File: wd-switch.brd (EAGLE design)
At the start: 35.2 x 57.1 mm, 13 parts, among them Q1 BC337, Q2 IRF530, Q3 IRF530

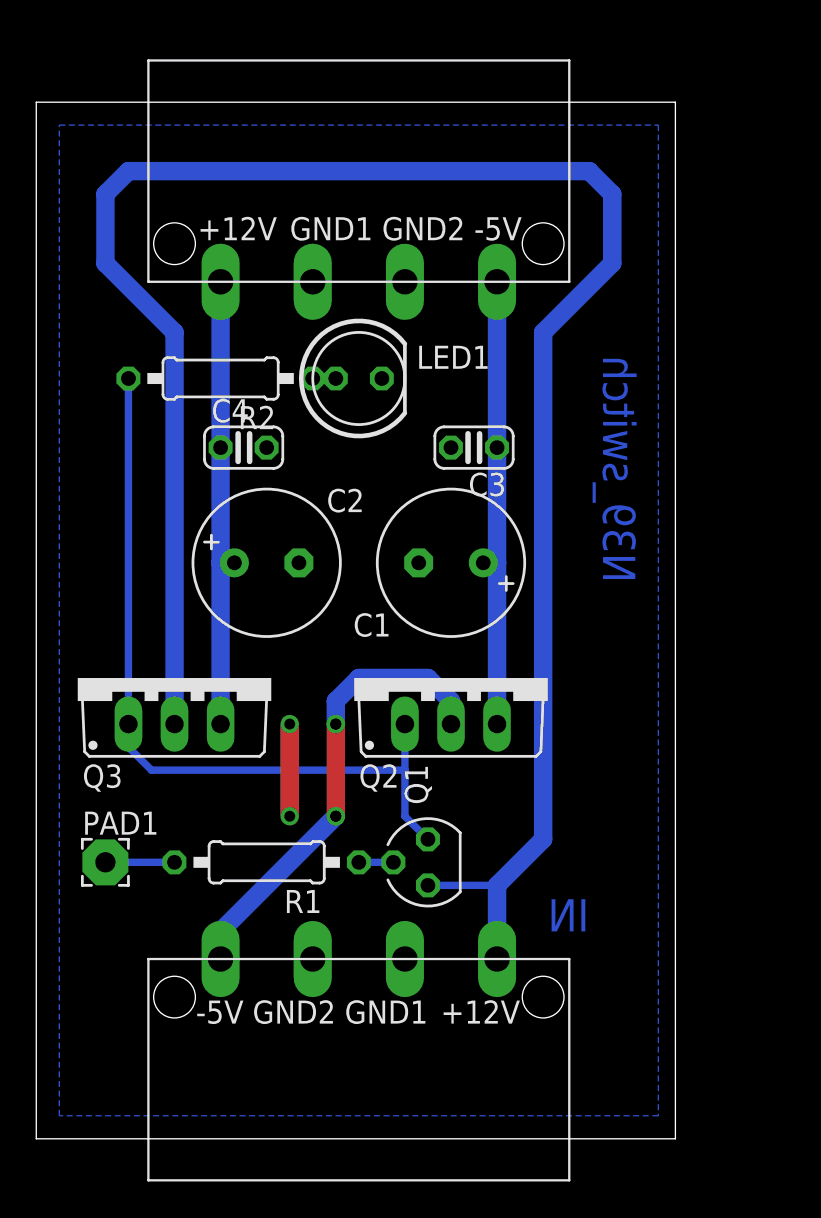
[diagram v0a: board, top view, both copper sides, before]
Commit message: * Bohrlöcher xD * kleine Verbesserungen im Platinenlayout
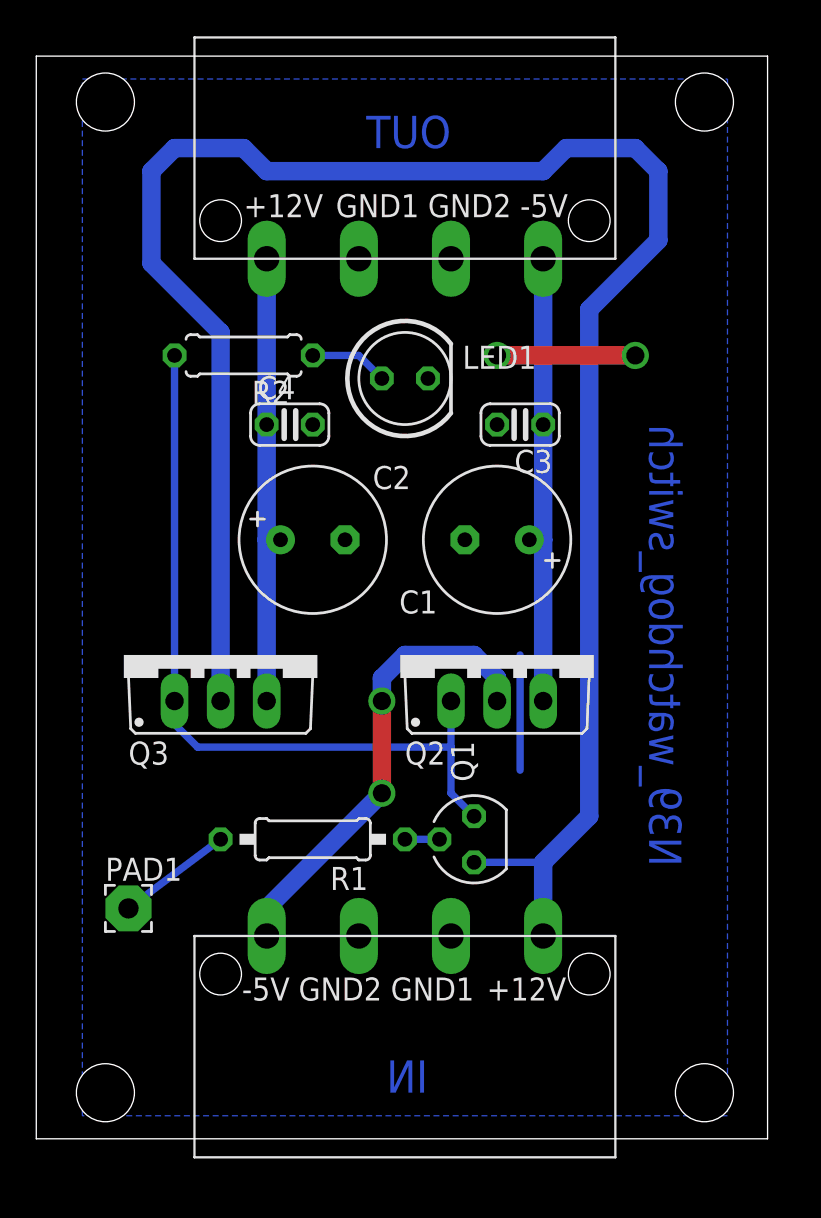
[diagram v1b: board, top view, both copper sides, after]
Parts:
- R2: device resistor:0207/10 -> resistor:0207/7
- moved C2 2.84 mm to (15.2, 33.0)
- moved R1 2.84 mm to (15.2, 16.5)
- moved Q3 2.84 mm to (10.2, 26.7)
- moved PAD1 2.84 mm to (5.08, 12.7)
- moved C1 2.84 mm to (25.4, 33.0)
- moved C3 2.84 mm to (26.7, 39.4)
- moved Q2 2.84 mm to (25.4, 26.7)
- moved Q1 2.84 mm to (24.1, 16.5)
- moved C4 2.84 mm to (14.0, 39.4)
- moved U$1 2.84 mm to (20.3, 5.08)
- moved U$2 2.84 mm to (20.3, 54.6)
- moved LED1 2.54 mm to (20.3, 41.9)
- moved R2 1.80 mm to (11.4, 43.2)
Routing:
- net GND: track 5.08 -> 14.0 mm
- net N$7: track 1.27 -> 4.34 mm
- net N$5: track 3.81 -> 6.35 mm
- net VCC: track 108.4 -> 109.4 mm
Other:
- board size 35.2 x 57.1 mm -> 40.3 x 59.7 mm
- board text added: "N39_watchdog_switch"
- board text added: "OUT"
- board text removed: "N39_switch"

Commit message: Pinheaders für statische Schalterstellung
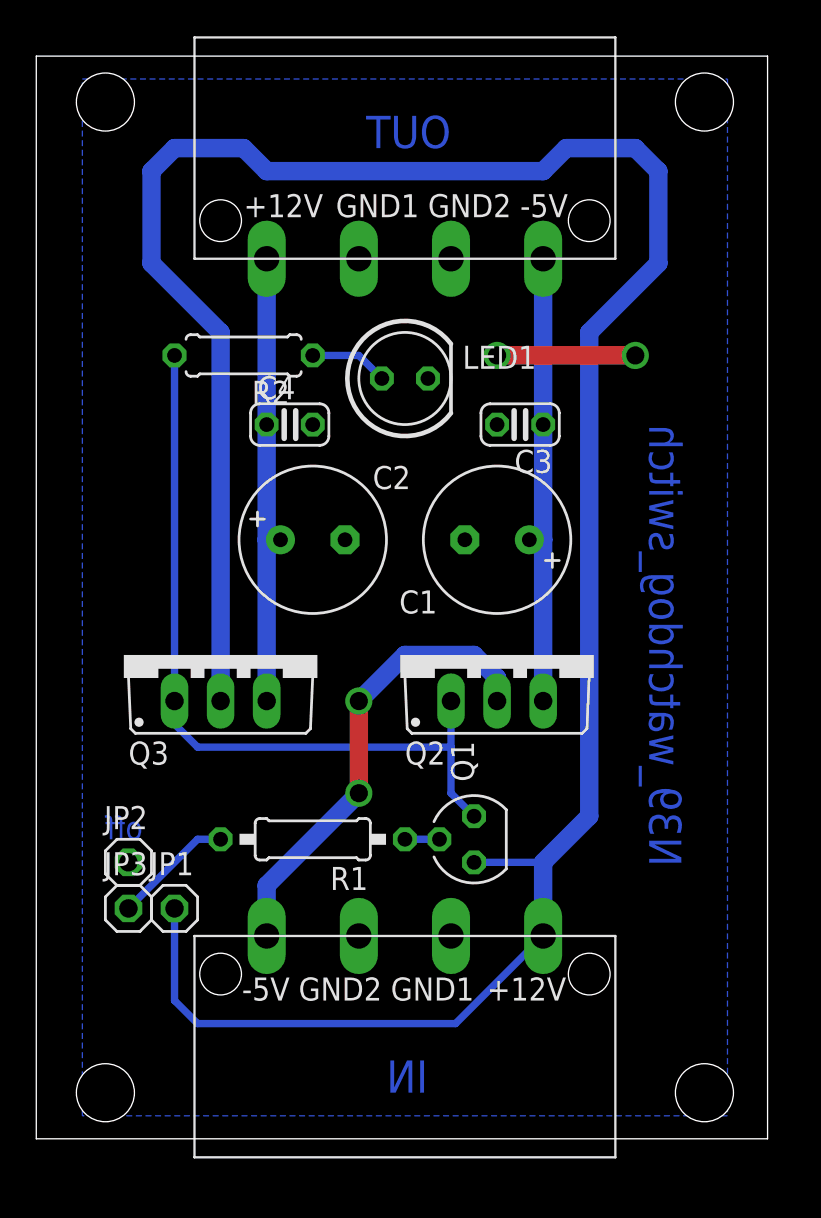
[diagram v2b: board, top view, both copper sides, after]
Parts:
- removed PAD1: WIREPAD2,54/1,1, wirepad:2,54/1,1
- added JP1: ON, pinhead:1X01
- added JP2: OFF, pinhead:1X01
- added JP3: IN, pinhead:1X01
- LED1: value (none) -> GN
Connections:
- net GND: now also JP2.1
- net N$5: now also JP3.1; no longer PAD1.1
- net VCC: now also JP1.1
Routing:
- net VCC: track 109.4 -> 137.4 mm
- net GND: track 14.0 -> 7.62 mm
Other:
- board text added: "off"
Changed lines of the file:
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@@
 <setting verticaltext="up"/>
 </settings>
-<grid distance="0.05" unitdist="inch" unit="inch" style="lines" multiple="1" display="no" altdistance="0.025" altunitdist="inch" altunit="inch"/>
+<grid distance="1.27" unitdist="mm" unit="mm" style="lines" multiple="1" display="no" altdistance="0.025" altunitdist="inch" altunit="inch"/>
 <layers>
 <layer number="1" name="Top" color="4" fill="1" visible="yes" active="yes"/>
@@
 <text x="22.86" y="54.61" size="1.778" layer="16" font="vector" rot="MR0">OUT</text>
 <text x="35.56" y="39.37" size="1.778" layer="16" font="vector" rot="MR270">N39_watchdog_switch</text>
+<text x="3.81" y="17.78" size="1.27" layer="16" font="vector" rot="MR180">off</text>
 </plain>
 <attributes>
@@
 <element name="U$2" library="n39" package="PSW_5" value="" x="20.32" y="54.61"/>
 <element name="R1" library="resistor" package="0207/10" value="330R" x="15.24" y="16.51" rot="R180"/>
-<element name="PAD1" library="wirepad" package="2,54/1,1" value="WIREPAD2,54/1,1" x="5.08" y="12.7"/>
-<element name="LED1" library="led" package="LED5MM" value="" x="20.32" y="41.91"/>
+<element name="LED1" library="led" package="LED5MM" value="GN" x="20.32" y="41.91"/>
 <element name="R2" library="resistor" package="0207/7" value="150R" x="11.43" y="43.18" rot="R180"/>
 <element name="C1" library="resistor" package="E3,5-8" value="" x="25.4" y="33.02" rot="R180"/>
@@
 <element name="C3" library="resistor" package="C025-024X044" value="" x="26.67" y="39.37" rot="R180"/>
 <element name="C4" library="resistor" package="C025-024X044" value="" x="13.97" y="39.37"/>
+<element name="JP1" library="pinhead" package="1X01" value="ON" x="7.62" y="12.7"/>
+<element name="JP2" library="pinhead" package="1X01" value="OFF" x="5.08" y="15.24"/>
+<element name="JP3" library="pinhead" package="1X01" value="IN" x="5.08" y="12.7"/>
 </elements>
 <signals>
@@
 <wire x1="6.35" y1="53.34" x2="7.62" y2="54.61" width="1.016" layer="16"/>
 <wire x1="33.02" y1="54.61" x2="34.29" y2="53.34" width="1.016" layer="16"/>
-<wire x1="34.29" y1="53.34" x2="34.29" y2="49.53" width="1.016" layer="16"/>
-<wire x1="34.29" y1="49.53" x2="30.48" y2="45.72" width="1.016" layer="16"/>
-<wire x1="30.48" y1="45.72" x2="30.48" y2="17.78" width="1.016" layer="16"/>
+<wire x1="34.29" y1="53.34" x2="34.29" y2="48.26" width="1.016" layer="16"/>
+<wire x1="34.29" y1="48.26" x2="30.48" y2="44.45" width="1.016" layer="16"/>
+<wire x1="30.48" y1="44.45" x2="30.48" y2="17.78" width="1.016" layer="16"/>
 <wire x1="30.48" y1="17.78" x2="27.94" y2="15.24" width="1.016" layer="16"/>
 <wire x1="27.94" y1="15.24" x2="27.94" y2="11.18" width="1.016" layer="16"/>
@@
 <wire x1="27.94" y1="53.34" x2="29.21" y2="54.61" width="1.016" layer="16"/>
 <wire x1="29.21" y1="54.61" x2="33.02" y2="54.61" width="1.016" layer="16"/>
+<contactref element="JP1" pad="1"/>
+<wire x1="7.62" y1="12.7" x2="7.62" y2="7.62" width="0.4064" layer="16"/>
+<wire x1="7.62" y1="7.62" x2="8.89" y2="6.35" width="0.4064" layer="16"/>
+<wire x1="8.89" y1="6.35" x2="23.11" y2="6.35" width="0.4064" layer="16"/>
+<wire x1="23.11" y1="6.35" x2="27.94" y2="11.18" width="0.4064" layer="16"/>
 </signal>
 <signal name="GND">
@@
 <via x="25.4" y="43.18" extent="1-16" drill="1" diameter="1.4224"/>
 <wire x1="25.4" y1="43.18" x2="33.02" y2="43.18" width="1.016" layer="1"/>
-<wire x1="26.67" y1="26.67" x2="26.67" y2="20.32" width="0.4064" layer="16"/>
+<contactref element="JP2" pad="1"/>
 </signal>
 <signal name="N$1">
@@
 <wire x1="25.4" y1="25.4" x2="24.13" y2="26.67" width="1.016" layer="16"/>
 <wire x1="24.13" y1="26.67" x2="20.32" y2="26.67" width="1.016" layer="16"/>
-<wire x1="20.32" y1="26.67" x2="19.05" y2="25.4" width="1.016" layer="16"/>
-<wire x1="19.05" y1="25.4" x2="19.05" y2="24.13" width="1.016" layer="16"/>
-<via x="19.05" y="24.13" extent="1-16" drill="0.6" shape="square"/>
-<wire x1="19.05" y1="24.13" x2="19.05" y2="19.05" width="1.016" layer="1"/>
-<via x="19.05" y="19.05" extent="1-16" drill="0.6" shape="square"/>
-<wire x1="19.05" y1="19.05" x2="12.7" y2="12.7" width="1.016" layer="16"/>
-<wire x1="12.7" y1="12.7" x2="12.7" y2="11.18" width="1.016" layer="16"/>
+<wire x1="20.32" y1="26.67" x2="17.78" y2="24.13" width="1.016" layer="16"/>
+<via x="17.78" y="24.13" extent="1-16" drill="0.6" shape="square"/>
+<wire x1="17.78" y1="24.13" x2="17.78" y2="19.05" width="1.016" layer="1"/>
+<via x="17.78" y="19.05" extent="1-16" drill="0.6" shape="square"/>
+<wire x1="17.78" y1="19.05" x2="12.7" y2="13.97" width="1.016" layer="16"/>
+<wire x1="12.7" y1="13.97" x2="12.7" y2="11.43" width="1.016" layer="16"/>
+<wire x1="12.7" y1="11.43" x2="12.7" y2="11.18" width="0" layer="19" extent="16-16"/>
 </signal>
 <signal name="N$2">
@@
 <wire x1="20.32" y1="16.51" x2="22.225" y2="16.51" width="0.4064" layer="16"/>
 </signal>
-<signal name="N$5">
-<contactref element="R1" pad="2"/>
-<contactref element="PAD1" pad="1"/>
-<wire x1="5.08" y1="12.7" x2="10.16" y2="16.51" width="0.4064" layer="16"/>
-</signal>
 <signal name="N$8">
 </signal>
@@
 <wire x1="17.78" y1="43.18" x2="19.05" y2="41.91" width="0.4064" layer="16"/>
 </signal>
-<signal name="N$11">
-<via x="19.05" y="24.13" extent="1-16" drill="1" diameter="1.4224"/>
-</signal>
-<signal name="N$12">
-<via x="19.05" y="19.05" extent="1-16" drill="1" diameter="1.4224"/>
+<signal name="N$5">
+<contactref element="R1" pad="2"/>
+<contactref element="JP3" pad="1"/>
+<wire x1="5.08" y1="12.7" x2="8.89" y2="16.51" width="0.4064" layer="16"/>
+<wire x1="8.89" y1="16.51" x2="10.16" y2="16.51" width="0.4064" layer="16"/>
+</signal>
+<signal name="N$6">
+<via x="17.78" y="24.13" extent="1-16" drill="1" diameter="1.4224"/>
+</signal>
+<signal name="N$9">
+<via x="17.78" y="19.05" extent="1-16" drill="1" diameter="1.4224"/>
 </signal>
 </signals>

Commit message: USB-Stromversorgung
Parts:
- added X1: KUSBVX, con-kycon:KUSBVX
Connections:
- net GND: now also X1.4
- net VCC: now also X1.1
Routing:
- net VCC: track 137.4 -> 143.8 mm
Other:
- board text added: "N39_wd_switch"
- board text removed: "N39_watchdog_switch"
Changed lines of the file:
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@@
 <setting verticaltext="up"/>
 </settings>
-<grid distance="1.27" unitdist="mm" unit="mm" style="lines" multiple="1" display="no" altdistance="0.025" altunitdist="inch" altunit="inch"/>
+<grid distance="0.05" unitdist="inch" unit="inch" style="lines" multiple="1" display="no" altdistance="0.025" altunitdist="inch" altunit="inch"/>
 <layers>
 <layer number="1" name="Top" color="4" fill="1" visible="yes" active="yes"/>
@@
 <hole x="3.81" y="57.15" drill="3.2"/>
 <text x="22.86" y="54.61" size="1.778" layer="16" font="vector" rot="MR0">OUT</text>
-<text x="35.56" y="39.37" size="1.778" layer="16" font="vector" rot="MR270">N39_watchdog_switch</text>
+<text x="38.1" y="48.26" size="1.778" layer="16" font="vector" rot="MR270">N39_wd_switch</text>
 <text x="3.81" y="17.78" size="1.27" layer="16" font="vector" rot="MR180">off</text>
 </plain>
@@
 <element name="JP2" library="pinhead" package="1X01" value="OFF" x="5.08" y="15.24"/>
 <element name="JP3" library="pinhead" package="1X01" value="IN" x="5.08" y="12.7"/>
+<element name="X1" library="con-kycon" package="KUSBVX" value="KUSBVX" x="34.29" y="19.05" rot="R270"/>
 </elements>
 <signals>
@@
 <wire x1="34.29" y1="53.34" x2="34.29" y2="48.26" width="1.016" layer="16"/>
 <wire x1="34.29" y1="48.26" x2="30.48" y2="44.45" width="1.016" layer="16"/>
-<wire x1="30.48" y1="44.45" x2="30.48" y2="17.78" width="1.016" layer="16"/>
-<wire x1="30.48" y1="17.78" x2="27.94" y2="15.24" width="1.016" layer="16"/>
-<wire x1="27.94" y1="15.24" x2="27.94" y2="11.18" width="1.016" layer="16"/>
-<wire x1="24.13" y1="15.24" x2="27.94" y2="15.24" width="0.4064" layer="16"/>
+<wire x1="30.48" y1="44.45" x2="30.48" y2="15.24" width="1.016" layer="16"/>
 <wire x1="7.62" y1="54.61" x2="11.43" y2="54.61" width="1.016" layer="16"/>
 <wire x1="11.43" y1="54.61" x2="12.7" y2="53.34" width="1.016" layer="16"/>
@@
 <wire x1="8.89" y1="6.35" x2="23.11" y2="6.35" width="0.4064" layer="16"/>
 <wire x1="23.11" y1="6.35" x2="27.94" y2="11.18" width="0.4064" layer="16"/>
+<contactref element="X1" pad="1"/>
+<wire x1="34.29" y1="15.55" x2="33.33" y2="15.55" width="1.016" layer="16"/>
+<wire x1="33.33" y1="15.55" x2="33.02" y2="15.24" width="1.016" layer="16"/>
+<wire x1="33.02" y1="15.24" x2="30.48" y2="15.24" width="1.016" layer="16"/>
+<wire x1="27.94" y1="11.18" x2="27.94" y2="12.7" width="1.016" layer="16"/>
+<wire x1="27.94" y1="12.7" x2="30.48" y2="15.24" width="1.016" layer="16"/>
+<wire x1="30.48" y1="15.24" x2="24.13" y2="15.24" width="0.4064" layer="16"/>
 </signal>
 <signal name="GND">
@@
 <wire x1="25.4" y1="43.18" x2="33.02" y2="43.18" width="1.016" layer="1"/>
 <contactref element="JP2" pad="1"/>
+<contactref element="X1" pad="4"/>
 </signal>
 <signal name="N$1">
@@
 </signal>
 </signals>
+<errors>
+</errors>
 </board>
 </drawing>

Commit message: Werte für die Kondensatoren angegeben
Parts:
- C1, C2: value (none) -> 470u
- C3, C4: value (none) -> 100n
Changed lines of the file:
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@@
 <element name="LED1" library="led" package="LED5MM" value="GN" x="20.32" y="41.91"/>
 <element name="R2" library="resistor" package="0207/7" value="150R" x="11.43" y="43.18" rot="R180"/>
-<element name="C1" library="resistor" package="E3,5-8" value="" x="25.4" y="33.02" rot="R180"/>
-<element name="C2" library="resistor" package="E3,5-8" value="" x="15.24" y="33.02"/>
-<element name="C3" library="resistor" package="C025-024X044" value="" x="26.67" y="39.37" rot="R180"/>
-<element name="C4" library="resistor" package="C025-024X044" value="" x="13.97" y="39.37"/>
+<element name="C1" library="resistor" package="E3,5-8" value="470u" x="25.4" y="33.02" rot="R180"/>
+<element name="C2" library="resistor" package="E3,5-8" value="470u" x="15.24" y="33.02"/>
+<element name="C3" library="resistor" package="C025-024X044" value="100n" x="26.67" y="39.37" rot="R180"/>
+<element name="C4" library="resistor" package="C025-024X044" value="100n" x="13.97" y="39.37"/>
 <element name="JP1" library="pinhead" package="1X01" value="ON" x="7.62" y="12.7"/>
 <element name="JP2" library="pinhead" package="1X01" value="OFF" x="5.08" y="15.24"/>

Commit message: Korrigiertes Design
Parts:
- removed Q2: IRF530, transistor-power:TO220BV
- added Q4: IRL540N, n39:TO220V
- added R3: 100R, resistor:0207/2V
- added R4: 100K, resistor:0207/2V
- Q3: value IRF530 -> IRL540N; device transistor-power:TO220BV -> n39:TO220V
- R1: value 330R -> 150R
- R2: device resistor:0207/7 -> resistor:0207/10
- moved Q3 14.0 mm to (24.1, 27.9)
- moved R1 1.27 mm to (16.5, 16.5)
- moved C2 1.27 mm to (14.0, 33.0)
- moved Q1 1.27 mm to (25.4, 16.5)
- moved R2 1.27 mm to (10.2, 43.2)
- renumbered U$1 to IN, U$2 to OUT
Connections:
- new net N$11: Q1.E, R2.2, R3.2
- net GND: now also R4.2
- net N$1: now also Q3.1, Q4.1, R3.1, R4.1; no longer Q1.E, Q2.G, Q3.G, R2.2
- net N$2: now also Q3.3; no longer Q2.S
- net N$4: now also OUT.+5V, Q4.3; no longer OUT.-5V, Q3.S
- net VCC: now also IN.+5V, Q4.2; no longer IN.-5V, Q3.D
- net VDD: now also Q3.2; no longer Q2.D
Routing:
- net N$11: track 0.00 -> 42.0 mm
- net N$1: track 43.0 -> 15.0 mm
- net VCC: track 143.8 -> 149.7 mm
- net VDD: track 25.3 -> 27.0 mm
- net N$5: track 6.66 -> 7.93 mm
- net N$4: track 25.1 -> 24.2 mm
- net N$2: track 25.1 -> 24.4 mm
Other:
- board text added: "on"
